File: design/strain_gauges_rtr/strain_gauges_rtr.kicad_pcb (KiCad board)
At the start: 2 copper layers, 88.9 x 44.5 mm, 40 parts, among them J1 Conn_01x03, J2 Conn_01x03, J3 Conn_01x08, J4 Conn_01x04, J5 Conn_01x04, J6 Conn_01x04, J7 Conn_01x04, P1 CONN_01X02, Q1 2N3096, U1 TL780-15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

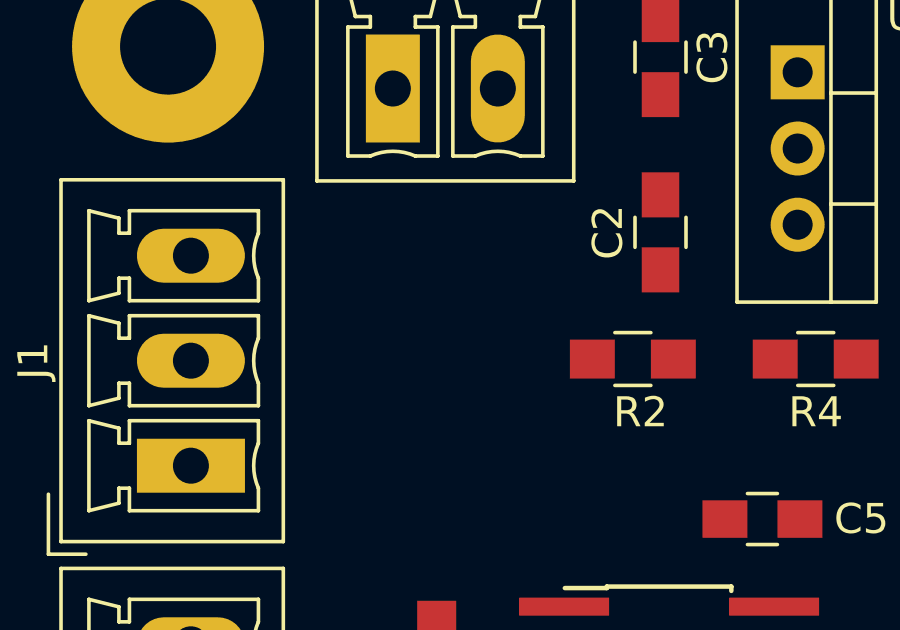
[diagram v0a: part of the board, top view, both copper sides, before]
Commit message: Add fuses to both strain gauge circuits.
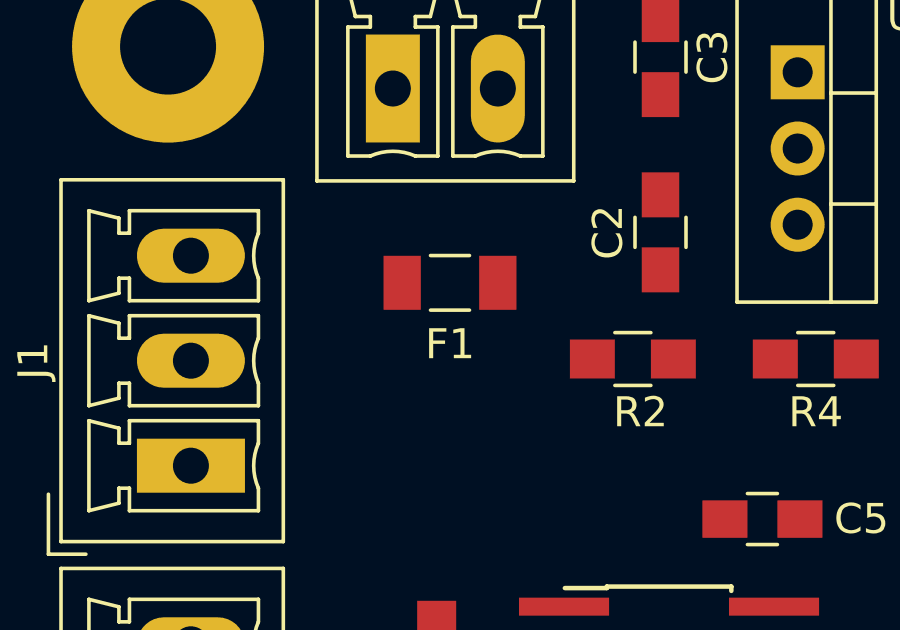
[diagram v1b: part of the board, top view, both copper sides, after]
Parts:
- added F1: Fuse, Fuse:Fuse_1206_3216Metric_Pad1.24x1.80mm_HandSolder, F.Cu at (105.2, 103.1)
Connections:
- P1 pad 2: +16V -> Net-(F1-Pad2)
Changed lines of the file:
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@@
 (kicad_pcb (version 4) (host pcbnew 4.0.7)
   (general
-    (links 82)
-    (no_connects 82)
-    (area 84.415143 89.332999 184.570858 134.561)
+    (links 83)
+    (no_connects 83)
+    (area 89.078999 89.332999 178.129001 133.933001)
     (thickness 1.6)
     (drawings 4)
     (tracks 0)
     (zones 0)
-    (modules 40)
-    (nets 34)
+    (modules 41)
+    (nets 35)
   )
   (page A4)
@@
   (net 32 "Net-(R12-Pad2)")
   (net 33 "Net-(R13-Pad2)")
+  (net 34 "Net-(F1-Pad2)")
   (net_class Default "This is the default net class."
     (clearance 0.2)
@@
     (add_net /STRAIN_OUT_4)
     (add_net GND)
+    (add_net "Net-(F1-Pad2)")
     (add_net "Net-(J3-Pad1)")
     (add_net "Net-(J3-Pad2)")
@@
       (net 2 GND))
     (pad 2 thru_hole oval (at 3.5 0) (size 1.8 3.6) (drill 1.2) (layers *.Cu *.Mask)
-      (net 1 +16V))
+      (net 34 "Net-(F1-Pad2)"))
     (model ${KISYS3DMOD}/Connectors_Phoenix.3dshapes/PhoenixContact_MCV-G_02x3.50mm_Vertical.wrl
       (at (xyz 0 0 0))
@@
     (pad 1 thru_hole circle (at 0 0) (size 6.4 6.4) (drill 3.2) (layers *.Cu *.Mask))
   )
+  (module Fuse:Fuse_1206_3216Metric_Pad1.24x1.80mm_HandSolder (layer F.Cu)
+    (at 105.156 103.124 180)
+    (descr "Fuse SMD 1206 (3216 Metric), square (rectangular) end terminal, IPC_7351 nominal with elongated pad for handsoldering. (Body size source: http://www.tortai-tech.com/upload/download/2011102023233369053.pdf), generated with kicad-footprint-generator")
+    (tags "resistor handsolder")
+    (attr smd)
+    (fp_text reference F1 (at 0 -2.05 180) (layer F.SilkS)
+      (effects (font (size 1 1) (thickness 0.15)))
+    )
+    (fp_text value Fuse (at 0 2.05 180) (layer F.Fab)
+      (effects (font (size 1 1) (thickness 0.15)))
+    )
+    (fp_line (start -1.6 0.8) (end -1.6 -0.8) (layer F.Fab) (width 0.1))
+    (fp_line (start -1.6 -0.8) (end 1.6 -0.8) (layer F.Fab) (width 0.1))
+    (fp_line (start 1.6 -0.8) (end 1.6 0.8) (layer F.Fab) (width 0.1))
+    (fp_line (start 1.6 0.8) (end -1.6 0.8) (layer F.Fab) (width 0.1))
+    (fp_line (start -0.65 -0.91) (end 0.65 -0.91) (layer F.SilkS) (width 0.12))
+    (fp_line (start -0.65 0.91) (end 0.65 0.91) (layer F.SilkS) (width 0.12))
+    (fp_line (start -2.46 1.15) (end -2.46 -1.15) (layer F.CrtYd) (width 0.05))
+    (fp_line (start -2.46 -1.15) (end 2.46 -1.15) (layer F.CrtYd) (width 0.05))
+    (fp_line (start 2.46 -1.15) (end 2.46 1.15) (layer F.CrtYd) (width 0.05))
+    (fp_line (start 2.46 1.15) (end -2.46 1.15) (layer F.CrtYd) (width 0.05))
+    (fp_text user %R (at 0 0 180) (layer F.Fab)
+      (effects (font (size 0.8 0.8) (thickness 0.12)))
+    )
+    (pad 1 smd rect (at -1.5925 0 180) (size 1.245 1.8) (layers F.Cu F.Paste F.Mask)
+      (net 1 +16V))
+    (pad 2 smd rect (at 1.5925 0 180) (size 1.245 1.8) (layers F.Cu F.Paste F.Mask)
+      (net 34 "Net-(F1-Pad2)"))
+    (model ${KISYS3DMOD}/Fuse.3dshapes/Fuse_1206_3216Metric.wrl
+      (at (xyz 0 0 0))
+      (scale (xyz 1 1 1))
+      (rotate (xyz 0 0 0))
+    )
+  )
   (gr_line (start 89.154 133.858) (end 178.054 133.858) (angle 90) (layer Edge.Cuts) (width 0.15))

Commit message: Finish routing on INA826 board.
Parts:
- moved R2 7.12 mm to (118.4, 105.9), turned to 180 degrees
- moved C3 6.03 mm to (112.8, 101.6), turned to 90 degrees
- moved C2 5.46 mm to (112.8, 96.0), turned to 270 degrees
- moved R4 5.09 mm to (112.3, 105.9), turned to 180 degrees
- moved REF** 0.51 mm to (173.2, 95.8)
- moved J4 0.38 mm to (113.5, 127.4)
- moved J5 0.38 mm to (130.8, 127.4)
- moved J6 0.38 mm to (148.1, 127.4)
- moved J7 0.38 mm to (165.4, 127.4)
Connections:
- J3 pad 3: /PRESSURE_2 -> /PRESSURE_1
- J3 pad 4: /PRESSURE_1 -> /PRESSURE_2
- J3 pad 5: /STRAIN_OUT_4 -> /STRAIN_OUT_1
- J3 pad 6: /STRAIN_OUT_3 -> /STRAIN_OUT_2
- J3 pad 7: /STRAIN_OUT_2 -> /STRAIN_OUT_3
- J3 pad 8: /STRAIN_OUT_1 -> /STRAIN_OUT_4
- U4 pad 7: /STRAIN_OUT_3 -> /STRAIN_OUT_2
- U5 pad 7: /STRAIN_OUT_2 -> /STRAIN_OUT_3
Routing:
- net +10V: track 0.00 -> 191.5 mm, vias 0 -> 4
- net /PRESSURE_2: track 0.00 -> 73.5 mm
- net GND: track 0.00 -> 68.4 mm, vias 0 -> 10
- net /PRESSURE_1: track 0.00 -> 61.0 mm
- net +16V: track 0.00 -> 54.3 mm
- net /STRAIN_OUT_1: track 0.00 -> 51.1 mm
- net +15V: track 0.00 -> 46.9 mm
- net Net-(J3-Pad2): track 0.00 -> 43.3 mm
- net /STRAIN_OUT_2: track 0.00 -> 36.1 mm
- net /STRAIN_OUT_3: track 0.00 -> 24.6 mm
- net /STRAIN_OUT_4: track 0.00 -> 22.3 mm
- net Net-(J3-Pad1): track 0.00 -> 18.8 mm
- net Net-(Q1-Pad2): track 0.00 -> 16.8 mm, vias 0 -> 1
- net Net-(J4-Pad2): track 0.00 -> 16.5 mm
- net Net-(J5-Pad2): track 0.00 -> 16.3 mm
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- added copper zone on B.Cu, net GND
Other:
- rule pad_to_mask_clearance: 0.2 -> 0.1016

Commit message: Finish silkscreen on INA826 board
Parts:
- added G***: LOGO, RLCS_footprints:rocketry_logo_small_noletters, F.Cu at (144.3, 105.5)
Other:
- board text added: "10V"
- board text added: "15V"
- board text added: "Alex Mihaila 09/04/19"
- board text added: "GND"
- board text added: "PANCAKE"
- board text added: "PWR"
- board text added: "S+"
- board text added: "S-"
- board text added: "S1"
- board text added: "S2"
- board text added: "S3"
- board text added: "S4"
- board text added: "S5"
- board text added: "S6"
- board text added: "SIGNAL OUT"
- board text added: "V1"
- board text added: "V2"
- board text added: "VO"

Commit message: Add most up to date rtr strain gauge files
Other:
- rule pad_to_mask_clearance: 0.1016 -> 0.0508
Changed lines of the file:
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@@
     (links 83)
     (no_connects 0)
-    (area 84.415143 89.713999 184.570858 134.561)
+    (area 84.415143 84.125 188.263675 134.561)
     (thickness 1.6)
-    (drawings 45)
+    (drawings 49)
     (tracks 269)
     (zones 0)
@@
     (pad_size 1.524 1.524)
     (pad_drill 0.762)
-    (pad_to_mask_clearance 0.1016)
+    (pad_to_mask_clearance 0.0508)
     (aux_axis_origin 0 0)
     (grid_origin 101.854 93.853)
     (visible_elements FFFEFF7F)
     (pcbplotparams
-      (layerselection 0x00030_80000001)
-      (usegerberextensions false)
-      (excludeedgelayer true)
+      (layerselection 0x010f0_80000001)
+      (usegerberextensions true)
+      (excludeedgelayer false)
       (linewidth 0.100000)
       (plotframeref false)
@@
       (outputformat 1)
       (mirror false)
-      (drillshape 1)
+      (drillshape 0)
       (scaleselection 1)
-      (outputdirectory ""))
+      (outputdirectory ../../fab/strain_gauges_rtr/))
   )
   (net 0 "")
@@
       (xy 0.007937 -4.808952) (xy 0.018053 -4.795405)) (layer F.SilkS) (width 0.01))
   )
+  (dimension 44.45 (width 0.15) (layer Eco1.User)
+    (gr_text "44.450 mm" (at 188.506 112.014 270) (layer Eco1.User)
+      (effects (font (size 1 1) (thickness 0.15)))
+    )
+    (feature1 (pts (xy 178.562 134.239) (xy 189.306 134.239)))
+    (feature2 (pts (xy 178.562 89.789) (xy 189.306 89.789)))
+    (crossbar (pts (xy 187.706 89.789) (xy 187.706 134.239)))
+    (arrow1a (pts (xy 187.706 134.239) (xy 187.119579 133.112496)))
+    (arrow1b (pts (xy 187.706 134.239) (xy 188.292421 133.112496)))
+    (arrow2a (pts (xy 187.706 89.789) (xy 187.119579 90.915504)))
+    (arrow2b (pts (xy 187.706 89.789) (xy 188.292421 90.915504)))
+  )
+  (dimension 89.154 (width 0.15) (layer Eco1.User)
+    (gr_text "89.154 mm" (at 134.239 80.607) (layer Eco1.User)
+      (effects (font (size 1 1) (thickness 0.15)))
+    )
+    (feature1 (pts (xy 178.816 90.043) (xy 178.816 79.807)))
+    (feature2 (pts (xy 89.662 90.043) (xy 89.662 79.807)))
+    (crossbar (pts (xy 89.662 81.407) (xy 178.816 81.407)))
+    (arrow1a (pts (xy 178.816 81.407) (xy 177.689496 81.993421)))
+    (arrow1b (pts (xy 178.816 81.407) (xy 177.689496 80.820579)))
+    (arrow2a (pts (xy 89.662 81.407) (xy 90.788504 81.993421)))
+    (arrow2b (pts (xy 89.662 81.407) (xy 90.788504 80.820579)))
+  )
+  (dimension 44.19673 (width 0.15) (layer Eco1.User)
+    (gr_text "1.7400 in" (at 184.573198 112.174817 89.67071754) (layer Eco1.User)
+      (effects (font (size 1 1) (thickness 0.15)))
+    )
+    (feature1 (pts (xy 178.562 134.239) (xy 185.246185 134.277415)))
+    (feature2 (pts (xy 178.816 90.043) (xy 185.500185 90.081415)))
+    (crossbar (pts (xy 183.900211 90.07222) (xy 183.646211 134.26822)))
+    (arrow1a (pts (xy 183.646211 134.26822) (xy 183.066274 133.138365)))
+    (arrow1b (pts (xy 183.646211 134.26822) (xy 184.239096 133.145105)))
+    (arrow2a (pts (xy 183.900211 90.07222) (xy 183.307326 91.195335)))
+    (arrow2b (pts (xy 183.900211 90.07222) (xy 184.480148 91.202075)))
+  )
+  (dimension 89.154 (width 0.15) (layer Eco1.User)
+    (gr_text "3.5100 in" (at 134.239 84.925) (layer Eco1.User)
+      (effects (font (size 1 1) (thickness 0.15)))
+    )
+    (feature1 (pts (xy 178.816 89.789) (xy 178.816 84.125)))
+    (feature2 (pts (xy 89.662 89.789) (xy 89.662 84.125)))
+    (crossbar (pts (xy 89.662 85.725) (xy 178.816 85.725)))
+    (arrow1a (pts (xy 178.816 85.725) (xy 177.689496 86.311421)))
+    (arrow1b (pts (xy 178.816 85.725) (xy 177.689496 85.138579)))
+    (arrow2a (pts (xy 89.662 85.725) (xy 90.788504 86.311421)))
+    (arrow2b (pts (xy 89.662 85.725) (xy 90.788504 85.138579)))
+  )
   (gr_text "Alex Mihaila\n09/04/19" (at 151.13 107.823) (layer F.SilkS)
